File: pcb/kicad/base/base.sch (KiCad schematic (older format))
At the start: 36 parts, among them J1 CHIP_EN, J2 Vbatt_I-test, P1 J-Link SWD, P2 SMA, P3 Power Source, U1 SAMB11G18A-edit, Y1 32.768kHz, Y2 26MHz

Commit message: Cleanup previous revision traces for new layout
Moving forward with full base station layout. Crystals, power caps, and
2.4GHz antenna placed. Mounting hole placements should coincide with
display mounting holes. May want to rotate XBee placement to allow push
buttons to be placed to the right of the display.
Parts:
- removed J1: CHIP_EN, Misc:Socket_Strip_Straight_1x02_Pitch2.54mm_Drill0.64mm, symbol CONN_01X02
- AE1: footprint (none) -> Antennas:Patch_Antenna_2.4GHz
- Y1: footprint Crystals:Crystal_C38-LF_d3.0mm_l8.0mm_Horizontal_1EP_style1 -> Crystals:Crystal_SMD_3215-2pin_3.2x1.5mm
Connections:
- wire segments 99 -> 100
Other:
- moved on the sheet: P2
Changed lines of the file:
@@
 L Antenna AE1
 U 1 1 58BAE3A5
-P 1675 2850
-F 0 "AE1" H 1600 2925 50  0000 R CNN
-F 1 "2.4-2.4835GHz" H 1600 2850 50  0000 R CNN
-F 2 "" H 1675 2850 50  0001 C CNN
-F 3 "" H 1675 2850 50  0001 C CNN
-	1    1675 2850
+P 2175 2750
+F 0 "AE1" H 2100 2825 50  0000 R CNN
+F 1 "2.4-2.4835GHz" H 2100 2750 50  0000 R CNN
+F 2 "Antennas:Patch_Antenna_2.4GHz" H 2175 2750 50  0001 C CNN
+F 3 "" H 2175 2750 50  0001 C CNN
+	1    2175 2750
 	1    0    0    -1
 $EndComp
@@
 $EndComp
 $Comp
-L GND #PWR019
-U 1 1 58BD31CE
-P 6050 5600
-F 0 "#PWR019" H 6050 5350 50  0001 C CNN
-F 1 "GND" H 6050 5475 50  0000 C CNN
-F 2 "" H 6050 5600 50  0000 C CNN
-F 3 "" H 6050 5600 50  0000 C CNN
-	1    6050 5600
-	1    0    0    -1
-$EndComp
-$Comp
 L CONN_01X02 J2
 U 1 1 58BD3D7F
@@
 $EndComp
 $Comp
-L GND #PWR020
+L GND #PWR019
 U 1 1 58BE3DF0
 P 4850 4700
-F 0 "#PWR020" H 4850 4450 50  0001 C CNN
+F 0 "#PWR019" H 4850 4450 50  0001 C CNN
 F 1 "GND" H 4850 4575 50  0000 C CNN
 F 2 "" H 4850 4700 50  0000 C CNN
@@
 $EndComp
 $Comp
-L GND #PWR021
+L GND #PWR020
 U 1 1 58BE3F81
 P 4450 4700
-F 0 "#PWR021" H 4450 4450 50  0001 C CNN
+F 0 "#PWR020" H 4450 4450 50  0001 C CNN
 F 1 "GND" H 4450 4575 50  0000 C CNN
 F 2 "" H 4450 4700 50  0000 C CNN
@@
 F 0 "Y1" H 4625 4100 50  0000 C CNN
 F 1 "32.768kHz" H 4625 3900 50  0000 C CNN
-F 2 "Crystals:Crystal_C38-LF_d3.0mm_l8.0mm_Horizontal_1EP_style1" H 4625 4000 50  0001 C CNN
+F 2 "Crystals:Crystal_SMD_3215-2pin_3.2x1.5mm" H 4625 4000 50  0001 C CNN
 F 3 "" H 4625 4000 50  0000 C CNN
 	1    4625 4000
@@
 L CONN_01X02 P2
 U 1 1 58BE1BD4
-P 1975 3100
-F 0 "P2" H 1975 3250 50  0000 C CNN
-F 1 "SMA" V 2075 3100 50  0000 C CNN
-F 2 "Misc:Molex_SMA_Jack_Edge_Mount" H 1975 3100 50  0001 C CNN
-F 3 "" H 1975 3100 50  0000 C CNN
-	1    1975 3100
+P 1875 3100
+F 0 "P2" H 1875 3250 50  0000 C CNN
+F 1 "SMA" V 1975 3100 50  0000 C CNN
+F 2 "Misc:Molex_SMA_Jack_Edge_Mount" H 1875 3100 50  0001 C CNN
+F 3 "" H 1875 3100 50  0000 C CNN
+	1    1875 3100
 	-1   0    0    -1
 $EndComp
 $Comp
-L GND #PWR022
+L GND #PWR021
 U 1 1 58BE519F
-P 2175 3150
-F 0 "#PWR022" H 2175 2900 50  0001 C CNN
-F 1 "GND" H 2175 3025 50  0000 C CNN
-F 2 "" H 2175 3150 50  0000 C CNN
-F 3 "" H 2175 3150 50  0000 C CNN
-	1    2175 3150
+P 2075 3150
+F 0 "#PWR021" H 2075 2900 50  0001 C CNN
+F 1 "GND" H 2075 3025 50  0000 C CNN
+F 2 "" H 2075 3150 50  0000 C CNN
+F 3 "" H 2075 3150 50  0000 C CNN
+	1    2075 3150
 	1    0    0    -1
 $EndComp
 NoConn ~ 5300 4600
 NoConn ~ 5350 4600
-$Comp
-L CONN_01X02 J1
-U 1 1 58BD2CFB
-P 5850 5550
-F 0 "J1" H 5850 5700 50  0000 C CNN
-F 1 "CHIP_EN" V 5950 5550 50  0000 C CNN
-F 2 "Misc:Socket_Strip_Straight_1x02_Pitch2.54mm_Drill0.64mm" H 5850 5550 50  0001 C CNN
-F 3 "" H 5850 5550 50  0000 C CNN
-	1    5850 5550
-	-1   0    0    -1
-$EndComp
 NoConn ~ 5525 4600
 NoConn ~ 5575 4600
@@
 DISP_B7
 $Comp
-L GND #PWR023
+L GND #PWR022
 U 1 1 58C42CEE
 P 6850 3150
-F 0 "#PWR023" H 6850 2900 50  0001 C CNN
+F 0 "#PWR022" H 6850 2900 50  0001 C CNN
 F 1 "GND" H 6850 3025 50  0000 C CNN
 F 2 "" H 6850 3150 50  0000 C CNN
@@
 $EndComp
 $Comp
-L GND #PWR024
+L GND #PWR023
 U 1 1 58C65889
 P 6850 2600
-F 0 "#PWR024" H 6850 2350 50  0001 C CNN
+F 0 "#PWR023" H 6850 2350 50  0001 C CNN
 F 1 "GND" H 6850 2475 50  0000 C CNN
 F 2 "" H 6850 2600 50  0000 C CNN
@@
 Text Label 6750 3750 0    30   ~ 0
 DISP_REG
+Wire Wire Line
+	2175 3050 2175 2950
 $EndSCHEMATC

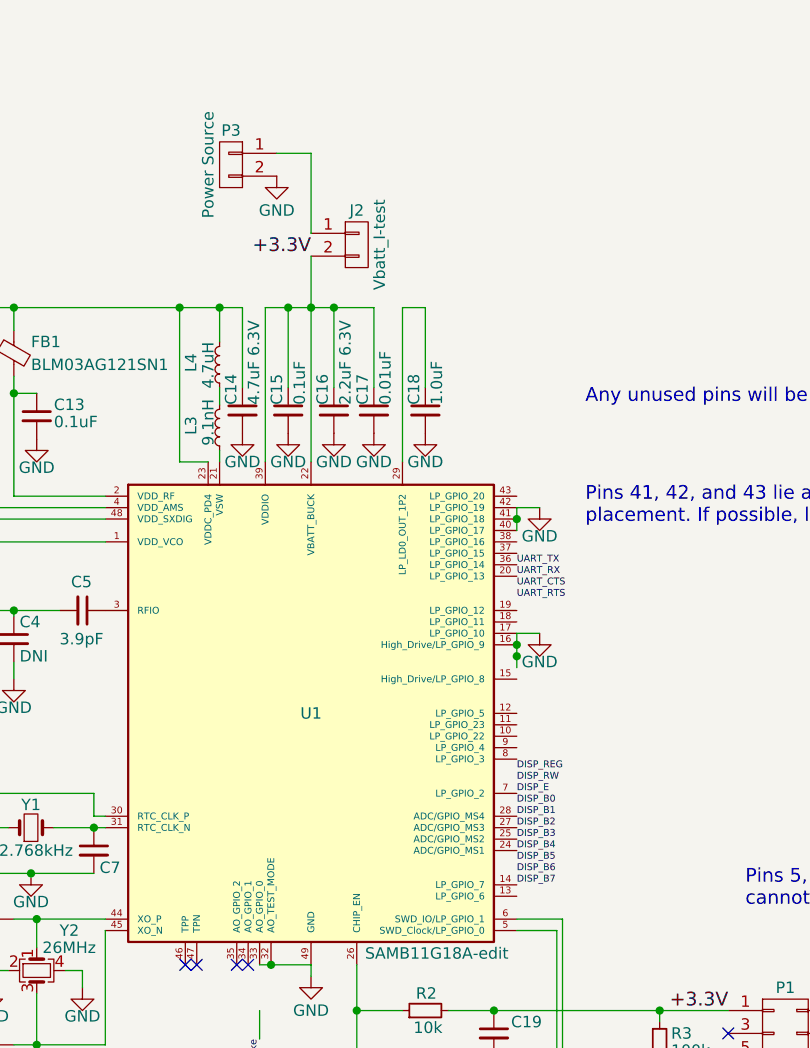
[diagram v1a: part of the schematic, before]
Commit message: Add initial display connections
Traces can be carefully placed underneath display footprint due to
elevated model. Patch antenna copper voids need to be understood.
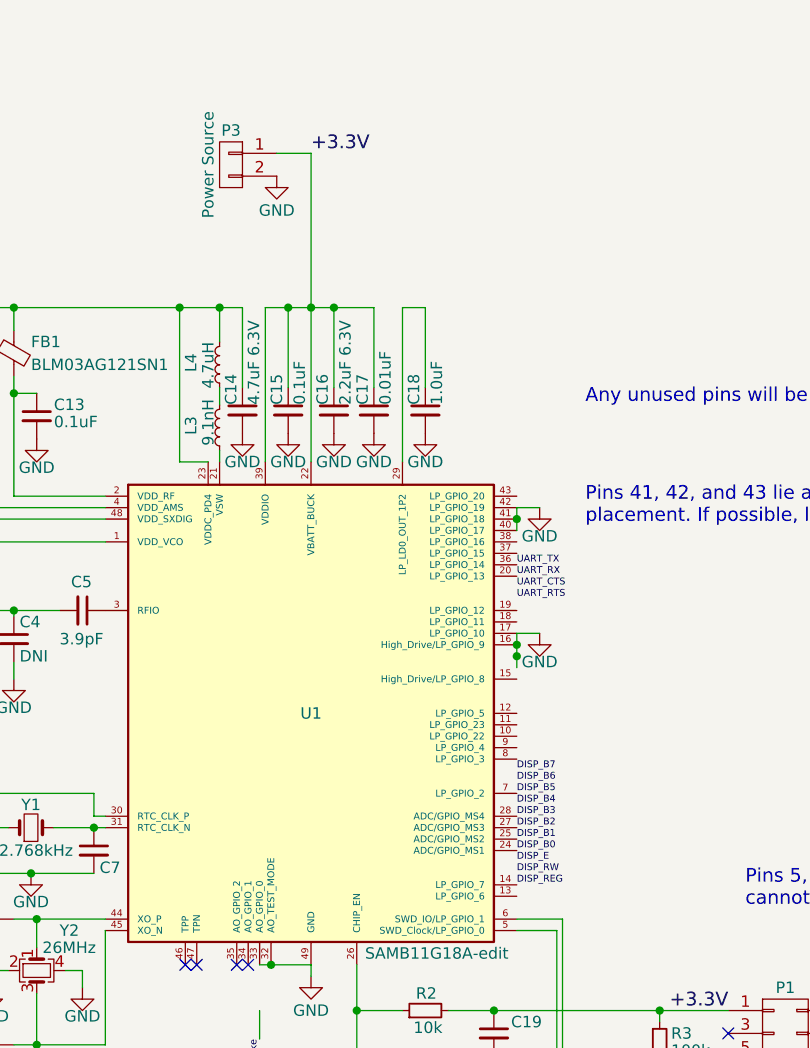
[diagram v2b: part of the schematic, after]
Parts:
- removed J2: Vbatt_I-test, Misc:Socket_Strip_Straight_1x02_Pitch2.54mm_Drill0.64mm, symbol CONN_01X02
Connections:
- wire segments 100 -> 99
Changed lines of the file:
@@
 	1    0    0    -1
 $EndComp
-Text Label 5850 1500 2    60   ~ 0
+Text Label 5850 1050 0    60   ~ 0
 +3.3V
 Text Label 2200 3050 0    60   ~ 0
@@
 Text Label 6750 2950 0    30   ~ 0
 UART_CTS
-Text Label 6750 4150 0    30   ~ 0
+Text Label 6750 3850 0    30   ~ 0
 DISP_B5
-Text Label 6750 4100 0    30   ~ 0
+Text Label 6750 3900 0    30   ~ 0
 DISP_B4
 Text Label 5625 4925 3    30   ~ 0
@@
 $EndComp
 $Comp
-L CONN_01X02 J2
-U 1 1 58BD3D7F
-P 6050 1450
-F 0 "J2" H 6050 1600 50  0000 C CNN
-F 1 "Vbatt_I-test" V 6150 1450 50  0000 C CNN
-F 2 "Misc:Socket_Strip_Straight_1x02_Pitch2.54mm_Drill0.64mm" H 6050 1450 50  0001 C CNN
-F 3 "" H 6050 1450 50  0000 C CNN
-	1    6050 1450
-	1    0    0    -1
-$EndComp
-$Comp
 L Crystal_GND24_Small Y2
 U 1 1 58BE100B
@@
 Text Label 6750 2900 0    30   ~ 0
 UART_RX
-Text Label 6750 3900 0    30   ~ 0
+Text Label 6750 4100 0    30   ~ 0
 DISP_B0
-Text Label 6750 3950 0    30   ~ 0
+Text Label 6750 4050 0    30   ~ 0
 DISP_B1
 Text Label 6750 4000 0    30   ~ 0
 DISP_B2
-Text Label 6750 4050 0    30   ~ 0
+Text Label 6750 3950 0    30   ~ 0
 DISP_B3
-Text Label 6750 4200 0    30   ~ 0
+Text Label 6750 3800 0    30   ~ 0
 DISP_B6
-Text Label 6750 4250 0    30   ~ 0
+Text Label 6750 3750 0    30   ~ 0
 DISP_B7
 $Comp
@@
 	6350 1725 6250 1725
 Wire Wire Line
-	5850 1500 5850 2400
-Wire Wire Line
-	5850 1050 5850 1400
+	5850 1050 5850 2400
 Wire Wire Line
 	5850 1050 5700 1050
@@
 Text Label 9850 2850 2    30   ~ 0
 DISP_E
-Text Label 6750 3850 0    30   ~ 0
+Text Label 6750 4150 0    30   ~ 0
 DISP_E
-Text Label 6750 3800 0    30   ~ 0
+Text Label 6750 4200 0    30   ~ 0
 DISP_RW
-Text Label 6750 3750 0    30   ~ 0
+Text Label 6750 4250 0    30   ~ 0
 DISP_REG
 Wire Wire Line

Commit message: Add new tests for patch antenna
Two new test boards laid out to test impedance and performance due to
the effect of larger copper void space in the presence of nearby ground
copper, one board with a matching circuit and the other without. Traces
no longer follow the optimal transmission line width for 50ohm
performance due to the use of 0402 SMD technology.
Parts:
- removed AE1: 2.4-2.4835GHz, Antennas:Patch_Antenna_2.4GHz, symbol Antenna
- added AE1: Antenna_Shield, Antennas:Patch_Antenna_2.4GHz, symbol Antenna_Shield
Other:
- moved on the sheet: P2
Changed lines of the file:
@@
-$EndComp
-$Comp
-L Antenna AE1
-U 1 1 58BAE3A5
-P 2175 2750
-F 0 "AE1" H 2100 2825 50  0000 R CNN
-F 1 "2.4-2.4835GHz" H 2100 2750 50  0000 R CNN
-F 2 "Antennas:Patch_Antenna_2.4GHz" H 2175 2750 50  0001 C CNN
-F 3 "" H 2175 2750 50  0001 C CNN
-	1    2175 2750
-	1    0    0    -1
 $EndComp
 $Comp
@@
 L CONN_01X02 P2
 U 1 1 58BE1BD4
-P 1875 3100
-F 0 "P2" H 1875 3250 50  0000 C CNN
-F 1 "SMA" V 1975 3100 50  0000 C CNN
-F 2 "Misc:Molex_SMA_Jack_Edge_Mount" H 1875 3100 50  0001 C CNN
-F 3 "" H 1875 3100 50  0000 C CNN
-	1    1875 3100
+P 1800 3100
+F 0 "P2" H 1800 3250 50  0000 C CNN
+F 1 "SMA" V 1900 3100 50  0000 C CNN
+F 2 "Misc:Molex_SMA_Jack_Edge_Mount" H 1800 3100 50  0001 C CNN
+F 3 "" H 1800 3100 50  0000 C CNN
+	1    1800 3100
 	-1   0    0    -1
 $EndComp
@@
 L GND #PWR021
 U 1 1 58BE519F
-P 2075 3150
-F 0 "#PWR021" H 2075 2900 50  0001 C CNN
-F 1 "GND" H 2075 3025 50  0000 C CNN
-F 2 "" H 2075 3150 50  0000 C CNN
-F 3 "" H 2075 3150 50  0000 C CNN
-	1    2075 3150
+P 2000 3150
+F 0 "#PWR021" H 2000 2900 50  0001 C CNN
+F 1 "GND" H 2000 3025 50  0000 C CNN
+F 2 "" H 2000 3150 50  0000 C CNN
+F 3 "" H 2000 3150 50  0000 C CNN
+	1    2000 3150
 	1    0    0    -1
 $EndComp
@@
 DISP_REG
 Wire Wire Line
-	2175 3050 2175 2950
+	2175 2750 2175 3050
+$Comp
+L Antenna_Shield AE1
+U 1 1 58E312C3
+P 2175 2550
+F 0 "AE1" H 2100 2725 50  0000 R CNN
+F 1 "Antenna_Shield" H 2100 2650 50  0000 R CNN
+F 2 "Antennas:Patch_Antenna_2.4GHz" H 2175 2650 50  0001 C CNN
+F 3 "" H 2175 2650 50  0001 C CNN
+	1    2175 2550
+	-1   0    0    -1
+$EndComp
+$Comp
+L GND #PWR?
+U 1 1 58E322FD
+P 2075 2750
+F 0 "#PWR?" H 2075 2500 50  0001 C CNN
+F 1 "GND" H 2075 2625 50  0000 C CNN
+F 2 "" H 2075 2750 50  0000 C CNN
+F 3 "" H 2075 2750 50  0000 C CNN
+	1    2075 2750
+	1    0    0    -1
+$EndComp
 $EndSCHEMATC

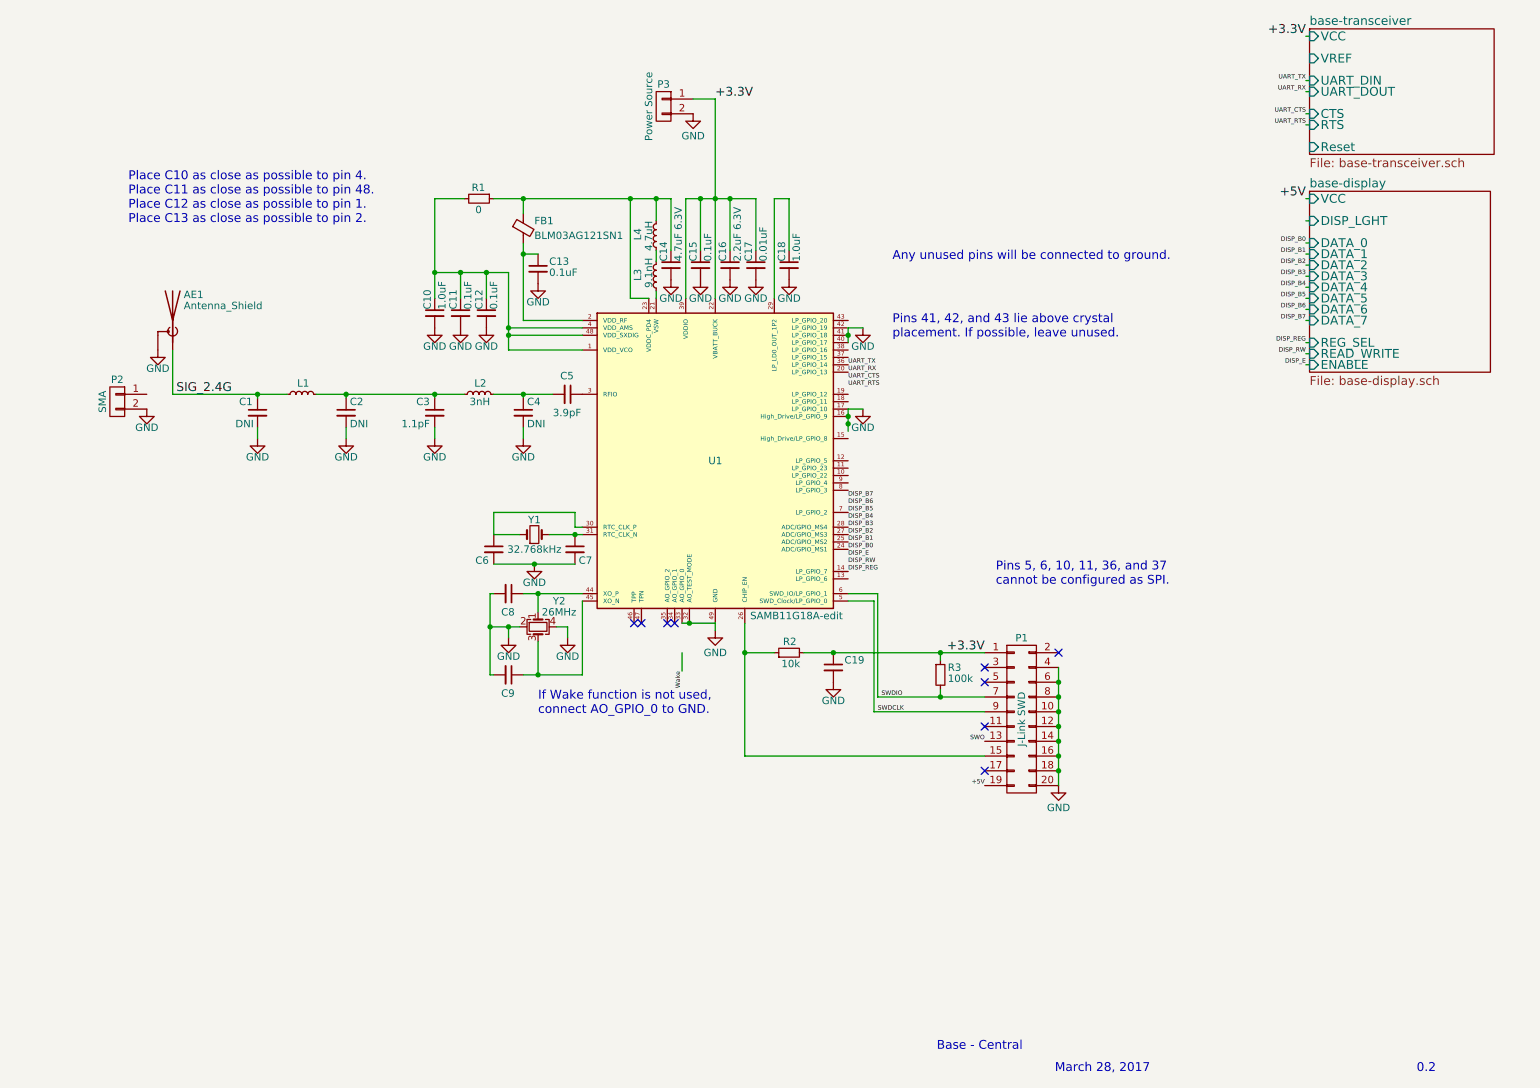
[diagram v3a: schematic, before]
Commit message: Update display and XBee position
Display is now placed on top of uC to shrink total package dimensions
and the XBee has been moved to accompany this change. Net vias have
been fixed to fit Bay Area Circuits' design constraints.
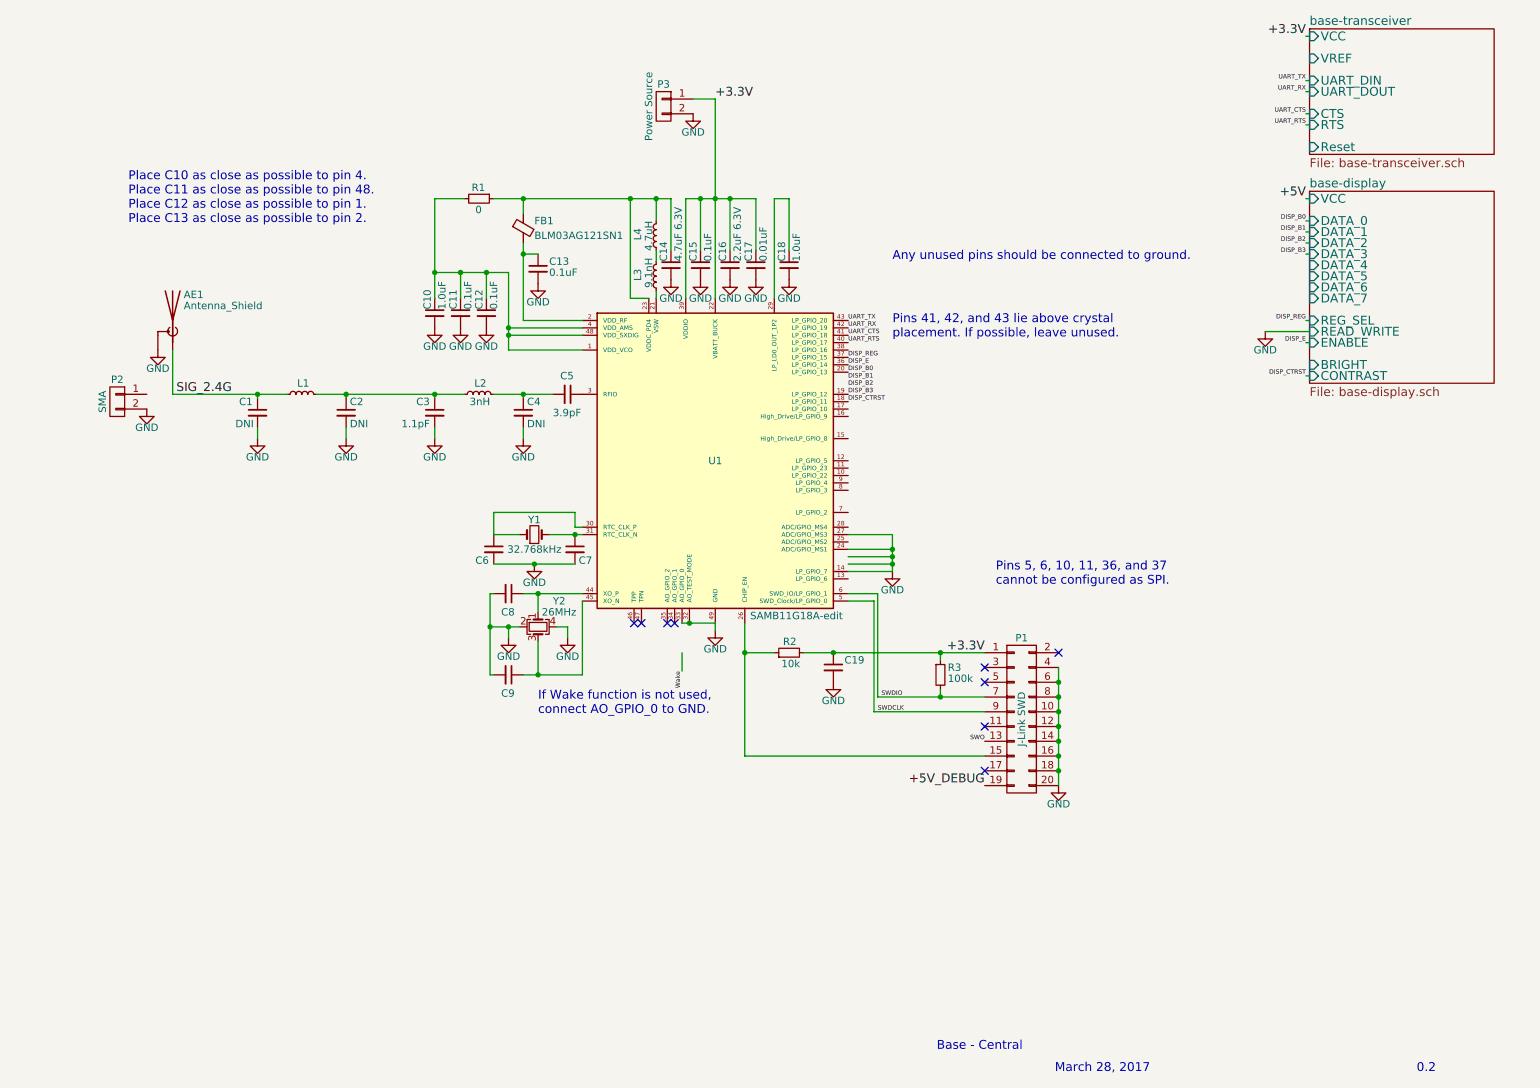
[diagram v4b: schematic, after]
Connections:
- net +5V: no longer P1.19 (P19)
- net DISP_B0: now also U1.20 (LP_GPIO_13); no longer U1.24 (ADC/GPIO_MS1)
- net DISP_B1: no longer U1.25 (ADC/GPIO_MS2)
- net DISP_B2: no longer U1.27 (ADC/GPIO_MS3)
- net DISP_B3: now also U1.19 (LP_GPIO_12); no longer U1.28 (ADC/GPIO_MS4)
- net DISP_E: now also U1.36 (LP_GPIO_14)
- net DISP_REG: now also U1.37 (LP_GPIO_15); no longer U1.14 (LP_GPIO_7)
- net GND: now also U1.14 (LP_GPIO_7), U1.24 (ADC/GPIO_MS1), U1.27 (ADC/GPIO_MS3); no longer U1.16 (High_Drive/LP_GPIO_9), U1.17 (LP_GPIO_10), U1.40 (LP_GPIO_17), U1.41 (LP_GPIO_18), U1.42 (LP_GPIO_19)
- net UART_CTS: now also U1.41 (LP_GPIO_18)
- net UART_RTS: now also U1.40 (LP_GPIO_17)
- net UART_RX: now also U1.42 (LP_GPIO_19); no longer U1.20 (LP_GPIO_13)
- net UART_TX: now also U1.43 (LP_GPIO_20); no longer U1.36 (LP_GPIO_14)
- net DISP_CTRST: now reaches U1.18 (LP_GPIO_11)
- net DISP_B5: no longer names the net of U1.7 (LP_GPIO_2)
- new net +5V_DEBUG: P1.19 (P19)
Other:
- note added: "Any unused pins should be connected to ground."
- note removed: "Any unused pins will be connected to ground."
